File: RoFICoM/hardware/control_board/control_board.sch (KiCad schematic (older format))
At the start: 26 parts, among them J1 Skirt Cable, J2 M+, J3 M-, J4 SWD, J5 DBG_UART, J6 SYS_CON, J7 SLIDER, U1 STM32G071GBU6, U2 DRV8837C, U3 BU52272NUZ, U4 MIC5365, U5 BU52272NUZ

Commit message: RoFICoM: Route ContorlBoard v0.2
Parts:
- added C8: 470n, Capacitor_SMD:C_0402_1005Metric, symbol Device:C
- J4: footprint Connector_PinHeader_1.27mm:PinHeader_1x05_P1.27mm_Vertical -> Connector_PinHeader_2.54mm:PinHeader_1x05_P2.54mm_Vertical
- J5: footprint Connector_PinHeader_1.27mm:PinHeader_1x03_P1.27mm_Vertical -> Connector_PinSocket_2.54mm:PinSocket_1x03_P2.54mm_Vertical
- J6: footprint Connector_PinHeader_1.27mm:PinHeader_1x07_P1.27mm_Vertical -> rofi:pogo_row_4_3
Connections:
- wire segments 21 -> 19
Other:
- moved on the sheet: C2, U5
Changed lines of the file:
@@
 L Device:C C2
 U 1 1 5C86BCA3
-P 6350 1550
-F 0 "C2" H 6465 1596 50  0000 L CNN
-F 1 "470n" H 6465 1505 50  0000 L CNN
-F 2 "Capacitor_SMD:C_0402_1005Metric" H 6388 1400 50  0001 C CNN
-F 3 "~" H 6350 1550 50  0001 C CNN
-	1    6350 1550
-	1    0    0    -1
-$EndComp
-Wire Wire Line
-	6500 1400 6350 1400
-Wire Wire Line
-	6350 1400 6250 1400
-Connection ~ 6350 1400
-$Comp
-L power:GND #PWR0108
-U 1 1 5C86BD54
-P 6350 1700
-F 0 "#PWR0108" H 6350 1450 50  0001 C CNN
-F 1 "GND" H 6355 1527 50  0000 C CNN
-F 2 "" H 6350 1700 50  0001 C CNN
-F 3 "" H 6350 1700 50  0001 C CNN
-	1    6350 1700
+P 2800 7000
+F 0 "C2" H 2915 7046 50  0000 L CNN
+F 1 "470n" H 2915 6955 50  0000 L CNN
+F 2 "Capacitor_SMD:C_0402_1005Metric" H 2838 6850 50  0001 C CNN
+F 3 "~" H 2800 7000 50  0001 C CNN
+	1    2800 7000
 	1    0    0    -1
 $EndComp
@@
 	0    1    1    0
 $EndComp
+Text GLabel 8150 3900 0    50   Input ~ 0
+MOTOR
 Text GLabel 8150 4000 0    50   Input ~ 0
-MOTOR
-Text GLabel 8150 3900 0    50   Input ~ 0
 MOTOR_PWM
 $Comp
@@
 L power:+3V3 #PWR0120
 U 1 1 5C86D9DD
-P 2750 7150
-F 0 "#PWR0120" H 2750 7000 50  0001 C CNN
-F 1 "+3V3" V 2765 7278 50  0000 L CNN
-F 2 "" H 2750 7150 50  0001 C CNN
-F 3 "" H 2750 7150 50  0001 C CNN
-	1    2750 7150
+P 3050 7150
+F 0 "#PWR0120" H 3050 7000 50  0001 C CNN
+F 1 "+3V3" V 3065 7278 50  0000 L CNN
+F 2 "" H 3050 7150 50  0001 C CNN
+F 3 "" H 3050 7150 50  0001 C CNN
+	1    3050 7150
 	0    1    1    0
 $EndComp
@@
 Text GLabel 1200 1600 0    50   Input ~ 0
 RST
-Text GLabel 1200 1500 0    50   Input ~ 0
-SDA
-Text GLabel 1200 1400 0    50   Input ~ 0
-SCL
 $Comp
 L Connector_Generic:Conn_01x05 J4
@@
 F 0 "J4" H 1480 1642 50  0000 L CNN
 F 1 "SWD" H 1480 1551 50  0000 L CNN
-F 2 "Connector_PinHeader_1.27mm:PinHeader_1x05_P1.27mm_Vertical" H 1400 1600 50  0001 C CNN
+F 2 "Connector_PinHeader_2.54mm:PinHeader_1x05_P2.54mm_Vertical" H 1400 1600 50  0001 C CNN
 F 3 "~" H 1400 1600 50  0001 C CNN
 	1    1400 1600
@@
 L rofi:BU52272NUZ U5
 U 1 1 5C86EF3E
-P 2250 6750
-F 0 "U5" H 2250 7025 50  0000 C CNN
-F 1 "BU52272NUZ" H 2250 6934 50  0000 C CNN
-F 2 "rofi:VSON04Z1114A" H 2250 6750 50  0001 C CNN
-F 3 "" H 2250 6750 50  0001 C CNN
-	1    2250 6750
+P 2250 6350
+F 0 "U5" H 2250 6625 50  0000 C CNN
+F 1 "BU52272NUZ" H 2250 6534 50  0000 C CNN
+F 2 "rofi:VSON04Z1114A" H 2250 6350 50  0001 C CNN
+F 3 "" H 2250 6350 50  0001 C CNN
+	1    2250 6350
 	1    0    0    -1
 $EndComp
@@
 L power:+3V3 #PWR0124
 U 1 1 5C86EF44
-P 2750 6700
-F 0 "#PWR0124" H 2750 6550 50  0001 C CNN
-F 1 "+3V3" V 2765 6828 50  0000 L CNN
-F 2 "" H 2750 6700 50  0001 C CNN
-F 3 "" H 2750 6700 50  0001 C CNN
-	1    2750 6700
+P 3050 6300
+F 0 "#PWR0124" H 3050 6150 50  0001 C CNN
+F 1 "+3V3" V 3065 6428 50  0000 L CNN
+F 2 "" H 3050 6300 50  0001 C CNN
+F 3 "" H 3050 6300 50  0001 C CNN
+	1    3050 6300
 	0    1    1    0
 $EndComp
@@
 L power:GND #PWR0125
 U 1 1 5C86EF4A
-P 2750 6800
-F 0 "#PWR0125" H 2750 6550 50  0001 C CNN
-F 1 "GND" V 2755 6672 50  0000 R CNN
-F 2 "" H 2750 6800 50  0001 C CNN
-F 3 "" H 2750 6800 50  0001 C CNN
-	1    2750 6800
-	0    -1   -1   0
-$EndComp
-Text GLabel 1750 6700 0    50   Input ~ 0
+P 2750 6400
+F 0 "#PWR0125" H 2750 6150 50  0001 C CNN
+F 1 "GND" V 2755 6272 50  0000 R CNN
+F 2 "" H 2750 6400 50  0001 C CNN
+F 3 "" H 2750 6400 50  0001 C CNN
+	1    2750 6400
+	0    -1   -1   0
+$EndComp
+Text GLabel 1750 6300 0    50   Input ~ 0
 LIMIT_1
 Text GLabel 1750 7150 0    50   Input ~ 0
 LIMIT_2
-NoConn ~ 1750 6800
+NoConn ~ 1750 6400
 NoConn ~ 1750 7250
-Text GLabel 7200 3400 2    50   Input ~ 0
+Text GLabel 4700 3900 0    50   Input ~ 0
 LIMIT_1
-Text GLabel 6700 3500 2    50   Input ~ 0
+Text GLabel 4700 3700 0    50   Input ~ 0
 LIMIT_2
-Wire Wire Line
-	7200 3400 7150 3400
-Wire Wire Line
-	7150 3300 7200 3300
-Wire Wire Line
-	7150 3300 7150 3400
-Connection ~ 7150 3400
-Wire Wire Line
-	7150 3400 6700 3400
-Text GLabel 7200 3300 2    50   Input ~ 0
+Text GLabel 6700 3200 2    50   Input ~ 0
 POT_SENSE
 $Comp
@@
 	1    0    0    -1
 $EndComp
+Text GLabel 4700 4950 0    50   Input ~ 0
+INT_SW
+Text GLabel 4700 4850 0    50   Input ~ 0
+INT_U
+Text GLabel 6700 3900 2    50   Input ~ 0
+INT_I
+Text GLabel 6700 3600 2    50   Input ~ 0
+EXT_SW
+Text GLabel 6700 3500 2    50   Input ~ 0
+EXT_U
+Text GLabel 6700 3400 2    50   Input ~ 0
+EXT_I
+Text GLabel 4700 4750 0    50   Input ~ 0
+SENSE_A
+Text GLabel 4700 4300 0    50   Input ~ 0
+SENSE_B
 Text GLabel 4700 3200 0    50   Input ~ 0
-INT_SW
-Text GLabel 4700 3700 0    50   Input ~ 0
-INT_U
-Text GLabel 4700 3900 0    50   Input ~ 0
-INT_I
-Text GLabel 4700 4300 0    50   Input ~ 0
-EXT_SW
-Text GLabel 6700 3200 2    50   Input ~ 0
-EXT_U
-Text GLabel 6700 3600 2    50   Input ~ 0
-EXT_I
-Text GLabel 6700 3900 2    50   Input ~ 0
-SENSE_A
-Text GLabel 4700 4750 0    50   Input ~ 0
-SENSE_B
-Text GLabel 4700 4850 0    50   Input ~ 0
 IN_U
 $Sheet
@@
 	0    -1   -1   0
 $EndComp
-Text Notes 1950 6400 0    50   ~ 0
+Text Notes 1950 6000 0    50   ~ 0
 Limit switches
 $Comp
@@
 F 0 "J5" H 2380 1742 50  0000 L CNN
 F 1 "DBG_UART" H 2380 1651 50  0000 L CNN
-F 2 "Connector_PinHeader_1.27mm:PinHeader_1x03_P1.27mm_Vertical" H 2300 1700 50  0001 C CNN
+F 2 "Connector_PinSocket_2.54mm:PinSocket_1x03_P2.54mm_Vertical" H 2300 1700 50  0001 C CNN
 F 3 "~" H 2300 1700 50  0001 C CNN
 	1    2300 1700
@@
 F 0 "J6" H 3930 1542 50  0000 L CNN
 F 1 "SYS_CON" H 3930 1451 50  0000 L CNN
-F 2 "Connector_PinHeader_1.27mm:PinHeader_1x07_P1.27mm_Vertical" H 3850 1500 50  0001 C CNN
+F 2 "rofi:pogo_row_4_3" H 3850 1500 50  0001 C CNN
 F 3 "~" H 3850 1500 50  0001 C CNN
 	1    3850 1500
 	1    0    0    -1
 $EndComp
-Text GLabel 3650 1800 0    50   Input ~ 0
+Text GLabel 3650 1300 0    50   Input ~ 0
 INT
-Text GLabel 3650 1700 0    50   Input ~ 0
+Text GLabel 3650 1200 0    50   Input ~ 0
 EXT
 $Comp
 L power:GND #PWR0145
 U 1 1 5C8876CF
-P 3650 1200
-F 0 "#PWR0145" H 3650 950 50  0001 C CNN
-F 1 "GND" V 3655 1072 50  0000 R CNN
-F 2 "" H 3650 1200 50  0001 C CNN
-F 3 "" H 3650 1200 50  0001 C CNN
-	1    3650 1200
+P 3650 1400
+F 0 "#PWR0145" H 3650 1150 50  0001 C CNN
+F 1 "GND" V 3655 1272 50  0000 R CNN
+F 2 "" H 3650 1400 50  0001 C CNN
+F 3 "" H 3650 1400 50  0001 C CNN
+	1    3650 1400
 	0    1    1    0
 $EndComp
@@
 L power:VCC #PWR0146
 U 1 1 5C887716
-P 3450 1300
-F 0 "#PWR0146" H 3450 1150 50  0001 C CNN
-F 1 "VCC" V 3468 1427 50  0000 L CNN
-F 2 "" H 3450 1300 50  0001 C CNN
-F 3 "" H 3450 1300 50  0001 C CNN
-	1    3450 1300
-	0    -1   -1   0
-$EndComp
-Wire Wire Line
-	3450 1300 3650 1300
-Text GLabel 3650 1400 0    50   Input ~ 0
+P 3650 1500
+F 0 "#PWR0146" H 3650 1350 50  0001 C CNN
+F 1 "VCC" V 3668 1627 50  0000 L CNN
+F 2 "" H 3650 1500 50  0001 C CNN
+F 3 "" H 3650 1500 50  0001 C CNN
+	1    3650 1500
+	0    -1   -1   0
+$EndComp
+Text GLabel 3650 1700 0    50   Input ~ 0
 SPI_SS
-Text GLabel 3650 1500 0    50   Input ~ 0
+Text GLabel 3650 1800 0    50   Input ~ 0
 SPI_SCK
 Text GLabel 3650 1600 0    50   Input ~ 0
@@
 	1    0    0    -1
 $EndComp
+Text GLabel 1200 1400 0    50   Input ~ 0
+SWCLK
+Text GLabel 1200 1500 0    50   Input ~ 0
+SWDIO
+Wire Wire Line
+	3050 6300 2800 6300
+Wire Wire Line
+	3050 7150 2800 7150
+$Comp
+L Device:C C8
+U 1 1 5C890AED
+P 2800 6150
+F 0 "C8" H 2915 6196 50  0000 L CNN
+F 1 "470n" H 2915 6105 50  0000 L CNN
+F 2 "Capacitor_SMD:C_0402_1005Metric" H 2838 6000 50  0001 C CNN
+F 3 "~" H 2800 6150 50  0001 C CNN
+	1    2800 6150
+	1    0    0    -1
+$EndComp
+Connection ~ 2800 6300
+Wire Wire Line
+	2800 6300 2750 6300
+$Comp
+L power:GND #PWR0108
+U 1 1 5C890C98
+P 2800 6000
+F 0 "#PWR0108" H 2800 5750 50  0001 C CNN
+F 1 "GND" V 2805 5872 50  0000 R CNN
+F 2 "" H 2800 6000 50  0001 C CNN
+F 3 "" H 2800 6000 50  0001 C CNN
+	1    2800 6000
+	-1   0    0    1
+$EndComp
+Connection ~ 2800 7150
+Wire Wire Line
+	2800 7150 2750 7150
+$Comp
+L power:GND #PWR0149
+U 1 1 5C890F51
+P 2800 6850
+F 0 "#PWR0149" H 2800 6600 50  0001 C CNN
+F 1 "GND" V 2805 6722 50  0000 R CNN
+F 2 "" H 2800 6850 50  0001 C CNN
+F 3 "" H 2800 6850 50  0001 C CNN
+	1    2800 6850
+	-1   0    0    1
+$EndComp
+Wire Wire Line
+	6250 1400 6500 1400
 $EndSCHEMATC

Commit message: RoFICoM: Fix wrong manufacture code of the voltage regulator
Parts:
- C1, C2, C3, C4, C5, C8: manf# (none) -> CC0402ZRY5V6BB474
- D1: manf# (none) -> 150060YS75000
- R1: manf# (none) -> RC0402JR-13220RL
- R12: manf# (none) -> RC0402JR-13100KL
- R13: manf# (none) -> RC0402FR-076K8L
- U1: manf# (none) -> STM32G071GBU6
- U2: manf# (none) -> DRV8837CDSGR
- U3, U5: manf# (none) -> BU52272NUZ-ZE2
- U4: manf# (none) -> MIC5365-3.3YMT-TZ
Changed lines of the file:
@@
 EESchema Schematic File Version 4
 LIBS:control_board-cache
-EELAYER 26 0
+EELAYER 29 0
 EELAYER END
 $Descr A4 11693 8268
@@
 F 2 "Package_DFN_QFN:UQFN-28-1EP_4x4mm_P0.4mm_EP2.35x2.35mm" H 5700 5075 50  0000 C CIN
 F 3 "" H 5700 3100 50  0000 C CNN
+F 4 "STM32G071GBU6" H 5700 4050 50  0001 C CNN "manf#"
 	1    5700 4050
 	1    0    0    -1
@@
 F 2 "Package_SON:WSON-8-1EP_2x2mm_P0.5mm_EP0.9x1.6mm" H 8750 4400 50  0001 C CNN
 F 3 "" H 8750 4400 50  0001 C CNN
+F 4 "DRV8837CDSGR" H 0   0   50  0001 C CNN "manf#"
 	1    8750 4100
 	1    0    0    -1
@@
 F 2 "rofi:VSON04Z1114A" H 2250 7200 50  0001 C CNN
 F 3 "" H 2250 7200 50  0001 C CNN
+F 4 "BU52272NUZ-ZE2" H 2250 7200 50  0001 C CNN "manf#"
 	1    2250 7200
 	1    0    0    -1
@@
 F 2 "rofi:MLF-4" H 5750 1400 50  0001 C CNN
 F 3 "" H 5750 1400 50  0001 C CNN
+F 4 "MIC5365-3.3YMT-TZ" H 0   0   50  0001 C CNN "manf#"
 	1    5750 1400
 	1    0    0    -1
@@
 F 2 "Capacitor_SMD:C_0402_1005Metric" H 7138 4600 50  0001 C CNN
 F 3 "~" H 7100 4750 50  0001 C CNN
+F 4 "CC0402ZRY5V6BB474" H 0   0   50  0001 C CNN "manf#"
 	1    7100 4750
 	1    0    0    -1
@@
 F 2 "Capacitor_SMD:C_0402_1005Metric" H 2838 6850 50  0001 C CNN
 F 3 "~" H 2800 7000 50  0001 C CNN
+F 4 "CC0402ZRY5V6BB474" H 0   0   50  0001 C CNN "manf#"
 	1    2800 7000
 	1    0    0    -1
@@
 F 2 "Capacitor_SMD:C_0402_1005Metric" H 5188 1400 50  0001 C CNN
 F 3 "~" H 5150 1550 50  0001 C CNN
+F 4 "CC0402ZRY5V6BB474" H 0   0   50  0001 C CNN "manf#"
 	1    5150 1550
 	1    0    0    -1
@@
 F 2 "Capacitor_SMD:C_0402_1005Metric" H 10088 3700 50  0001 C CNN
 F 3 "~" H 10050 3850 50  0001 C CNN
+F 4 "CC0402ZRY5V6BB474" H 0   0   50  0001 C CNN "manf#"
 	1    10050 3850
 	1    0    0    -1
@@
 F 2 "Capacitor_SMD:C_0402_1005Metric" H 9388 3600 50  0001 C CNN
 F 3 "~" H 9350 3750 50  0001 C CNN
+F 4 "CC0402ZRY5V6BB474" H 0   0   50  0001 C CNN "manf#"
 	1    9350 3750
 	1    0    0    -1
@@
 F 2 "rofi:VSON04Z1114A" H 2250 6350 50  0001 C CNN
 F 3 "" H 2250 6350 50  0001 C CNN
+F 4 "BU52272NUZ-ZE2" H 2250 6350 50  0001 C CNN "manf#"
 	1    2250 6350
 	1    0    0    -1
@@
 F 2 "LED_SMD:LED_0603_1608Metric" H 7400 1300 50  0001 C CNN
 F 3 "~" H 7400 1300 50  0001 C CNN
+F 4 "150060YS75000" H 0   0   50  0001 C CNN "manf#"
 	1    7400 1300
 	0    -1   -1   0
@@
 F 2 "Resistor_SMD:R_0402_1005Metric" V 7330 1600 50  0001 C CNN
 F 3 "~" H 7400 1600 50  0001 C CNN
+F 4 "RC0402JR-13220RL" H 0   0   50  0001 C CNN "manf#"
 	1    7400 1600
 	1    0    0    -1
@@
 F 2 "Resistor_SMD:R_0402_1005Metric" V 1030 3600 50  0001 C CNN
 F 3 "~" H 1100 3600 50  0001 C CNN
+F 4 "RC0402JR-13100KL" H 0   0   50  0001 C CNN "manf#"
 	1    1100 3600
 	1    0    0    -1
@@
 F 2 "Resistor_SMD:R_0402_1005Metric" V 1030 3900 50  0001 C CNN
 F 3 "~" H 1100 3900 50  0001 C CNN
+F 4 "RC0402FR-076K8L" H 0   0   50  0001 C CNN "manf#"
 	1    1100 3900
 	1    0    0    -1
@@
 F 2 "Capacitor_SMD:C_0402_1005Metric" H 2838 6000 50  0001 C CNN
 F 3 "~" H 2800 6150 50  0001 C CNN
+F 4 "CC0402ZRY5V6BB474" H 0   0   50  0001 C CNN "manf#"
 	1    2800 6150
 	1    0    0    -1

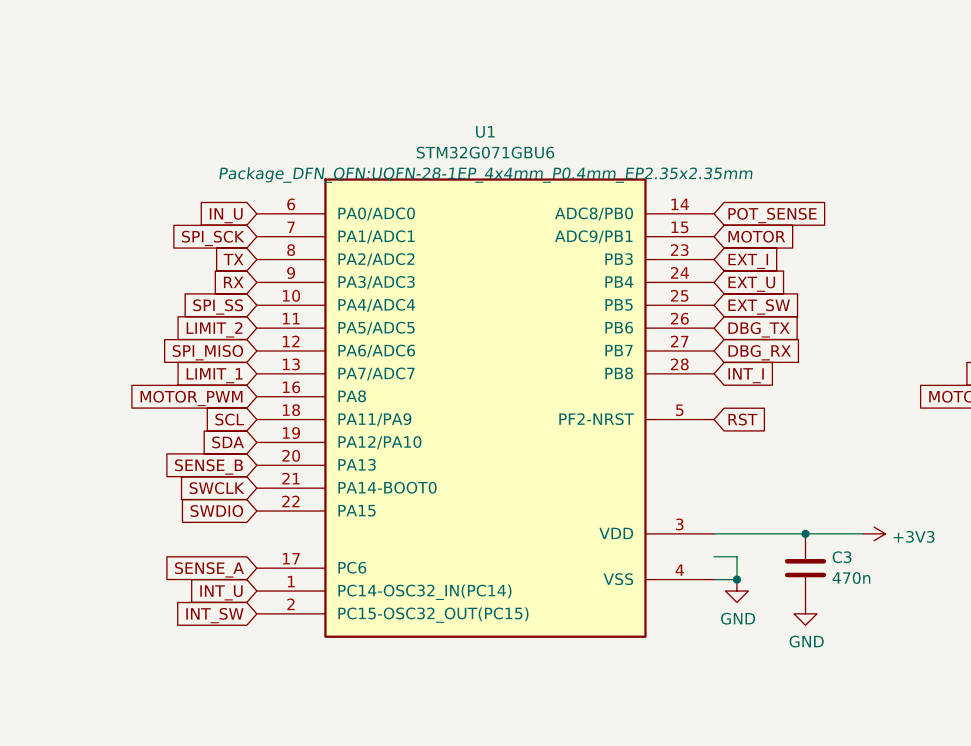
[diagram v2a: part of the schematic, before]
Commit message: RoFICoM: Change footprint of the MCU
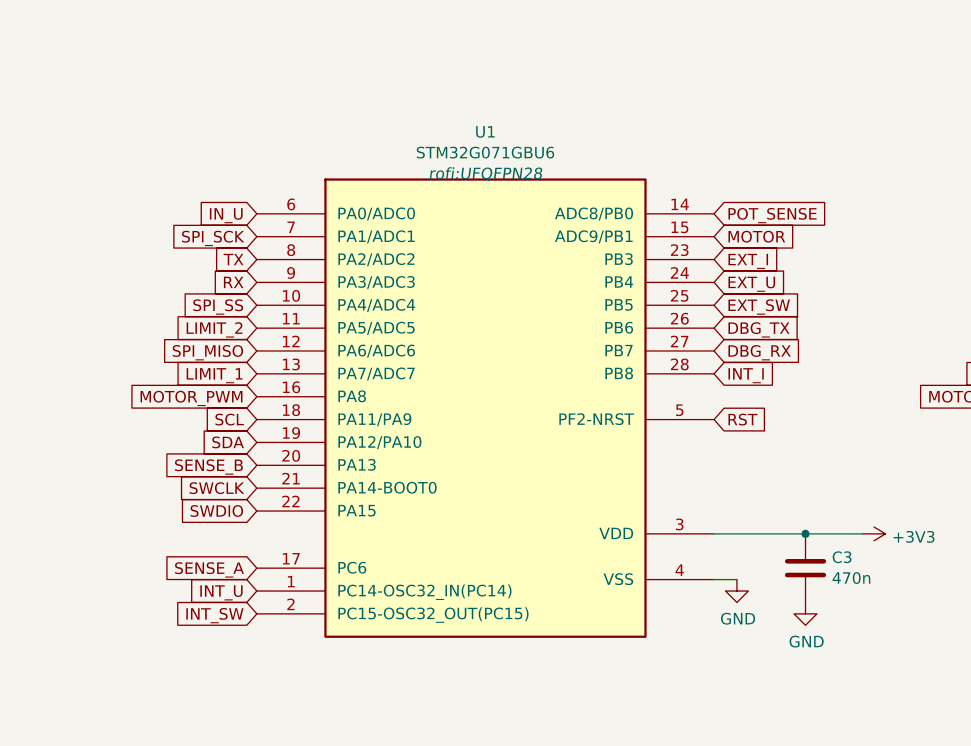
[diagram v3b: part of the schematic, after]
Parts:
- U1: footprint Package_DFN_QFN:UQFN-28-1EP_4x4mm_P0.4mm_EP2.35x2.35mm -> rofi:UFQFPN28
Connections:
- wire segments 19 -> 17
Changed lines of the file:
@@
 F 0 "U1" H 5700 5257 50  0000 C CNN
 F 1 "STM32G071GBU6" H 5700 5166 50  0000 C CNN
-F 2 "Package_DFN_QFN:UQFN-28-1EP_4x4mm_P0.4mm_EP2.35x2.35mm" H 5700 5075 50  0000 C CIN
+F 2 "rofi:UFQFPN28" H 5700 5075 50  0000 C CIN
 F 3 "" H 5700 3100 50  0000 C CNN
 F 4 "STM32G071GBU6" H 5700 4050 50  0001 C CNN "manf#"
@@
 MOTOR
 Wire Wire Line
-	6700 4700 6800 4700
-Wire Wire Line
-	6800 4700 6800 4800
-Wire Wire Line
 	6800 4800 6700 4800
 $Comp
@@
 	1    0    0    -1
 $EndComp
-Connection ~ 6800 4800
 $Comp
 L power:+3V3 #PWR0102
